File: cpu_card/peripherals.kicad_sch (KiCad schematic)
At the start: 23 parts, among them J301 UART1, J302 UART2, J303 USB B, SW301 CLR, U301 SC16C752B, U302 FT231XS, U303 DS12885T, Y301 18.432MHz, Y302 32.768kHz

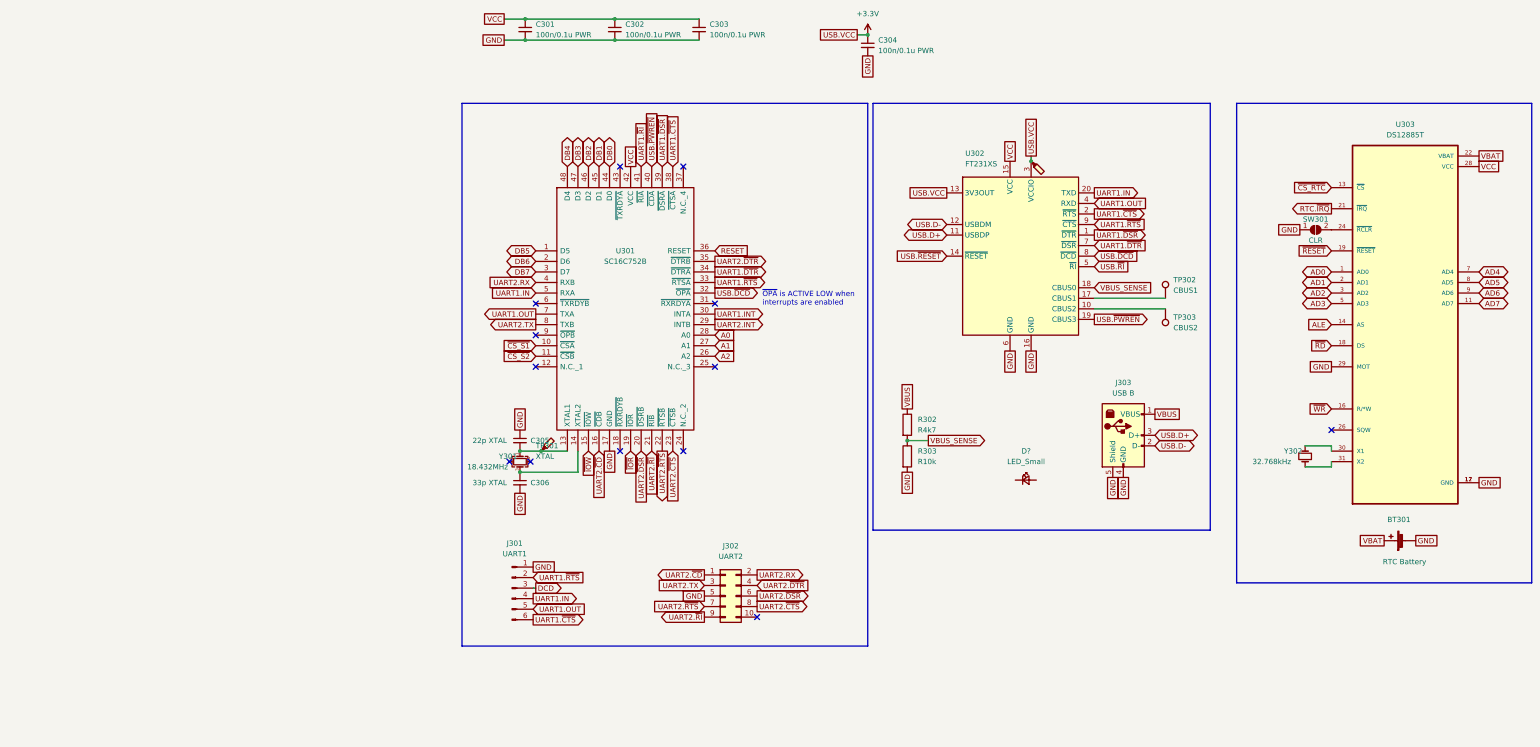
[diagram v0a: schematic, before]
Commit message: bios library and overall cleanup
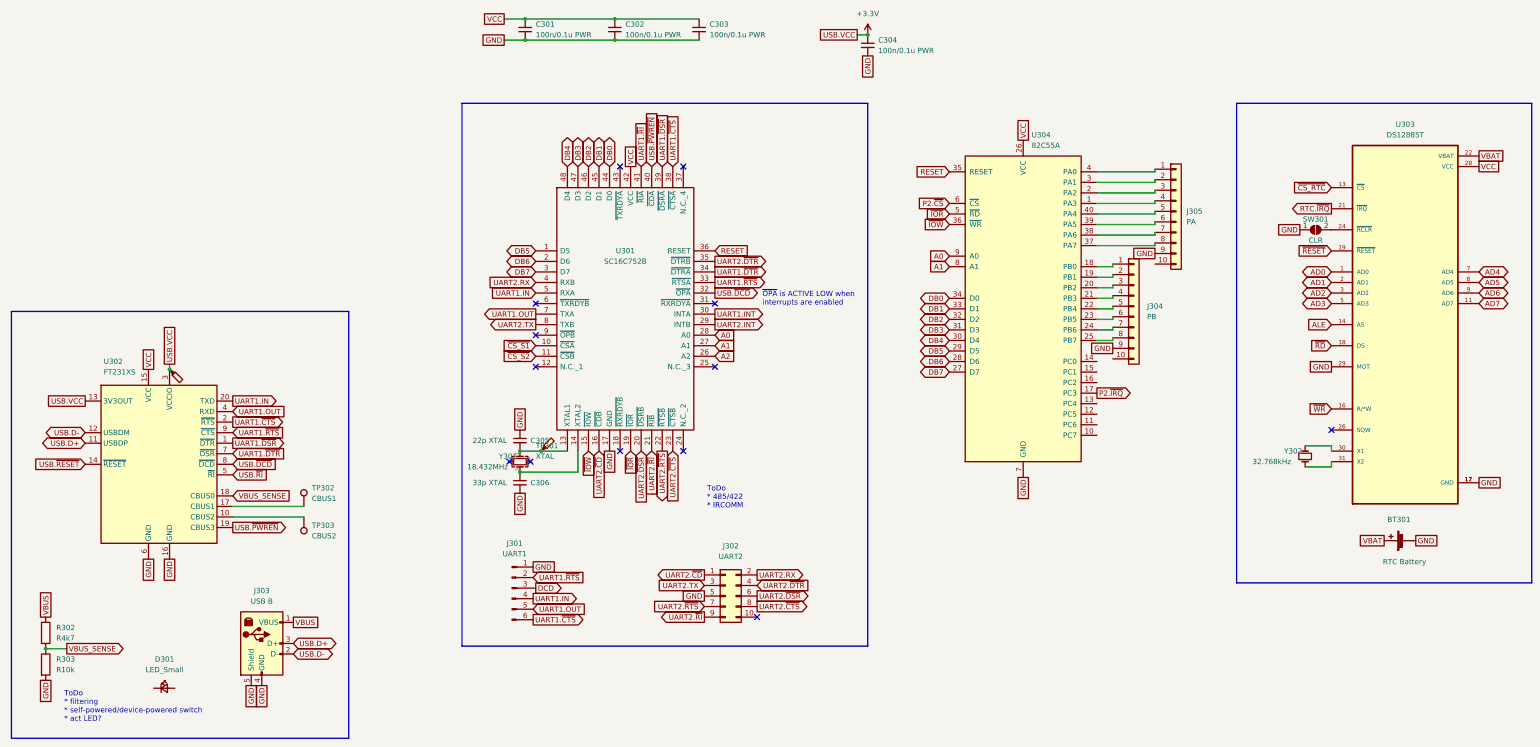
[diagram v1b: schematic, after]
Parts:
- added J304: PB, Connector_PinHeader_1.27mm:PinHeader_2x05_P1.27mm_Vertical, symbol Connector_Generic:Conn_01x10
- added J305: PA, Connector_PinHeader_1.27mm:PinHeader_2x05_P1.27mm_Vertical, symbol Connector_Generic:Conn_01x10
- added U304: 82C55A, Package_SO:TSSOP-40_6.1x11mm_P0.5mm, symbol Interface:82C55A
- J302: footprint Connector_PinSocket_1.27mm:PinSocket_2x05_P1.27mm_Vertical -> Connector_PinHeader_1.27mm:PinHeader_2x05_P1.27mm_Vertical
- gave numbers to parts that had none: 2
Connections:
- net A0: now also U304.9 (A0)
- net A1: now also U304.8 (A1)
- net DB0: now also U304.34 (D0)
- net DB1: now also U304.33 (D1)
- net DB2: now also U304.32 (D2)
- net DB3: now also U304.31 (D3)
- net DB4: now also U304.30 (D4)
- net DB5: now also U304.29 (D5)
- net DB6: now also U304.28 (D6)
- net DB7: now also U304.27 (D7)
- net GND: now also J304.9 (Pin_9), J305.9 (Pin_9), U304.7 (GND)
- net RESET: now also U304.35 (RESET)
- net VCC: now also U304.26 (VCC)
- net ~{IOR}: now also U304.5 (~{RD})
- net ~{IOW}: now also U304.36 (~{WR})
- new net: J305.4 (Pin_4), U304.1 (PA3)
- new net: J304.1 (Pin_1), U304.18 (PB0)
- new net: J304.2 (Pin_2), U304.19 (PB1)
- new net: J305.3 (Pin_3), U304.2 (PA2)
- new net: J304.3 (Pin_3), U304.20 (PB2)
- new net: J304.4 (Pin_4), U304.21 (PB3)
- new net: J304.5 (Pin_5), U304.22 (PB4)
- new net: J304.6 (Pin_6), U304.23 (PB5)
- new net: J304.7 (Pin_7), U304.24 (PB6)
- new net: J304.8 (Pin_8), U304.25 (PB7)
- new net: J305.2 (Pin_2), U304.3 (PA1)
- new net: J305.8 (Pin_8), U304.37 (PA7)
- new net: J305.7 (Pin_7), U304.38 (PA6)
- new net: J305.6 (Pin_6), U304.39 (PA5)
- new net: J305.1 (Pin_1), U304.4 (PA0)
- new net: J305.5 (Pin_5), U304.40 (PA4)
- new net P2.~{CS}: U304.6 (~{CS})
- new net P2.~{IRQ}: U304.17 (PC3)
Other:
- note added: "ToDo * 485/422 * IRCOMM"
- note added: "ToDo * filtering * self-powered/device-powered switch * act LED?"
- moved on the sheet: D301, J303, R302, R303, TP302, TP303, U302
